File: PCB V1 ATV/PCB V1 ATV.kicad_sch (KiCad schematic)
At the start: 19 parts, among them J1 Power, J10 NW Sensor, J11 N Sensor, J12 NE Sensor, J13 SW Sensor, J14 S Sensor, J15 SE Sensor, J16 Joystick, J17 MotorControl, J2 PWM, J3 Analog, J4 PWM, J5 Analog, J6 Communication, J7 Digital, J8 Battery 12vIN, J9 Motor Controller, SW1 EStop, U1 L7809

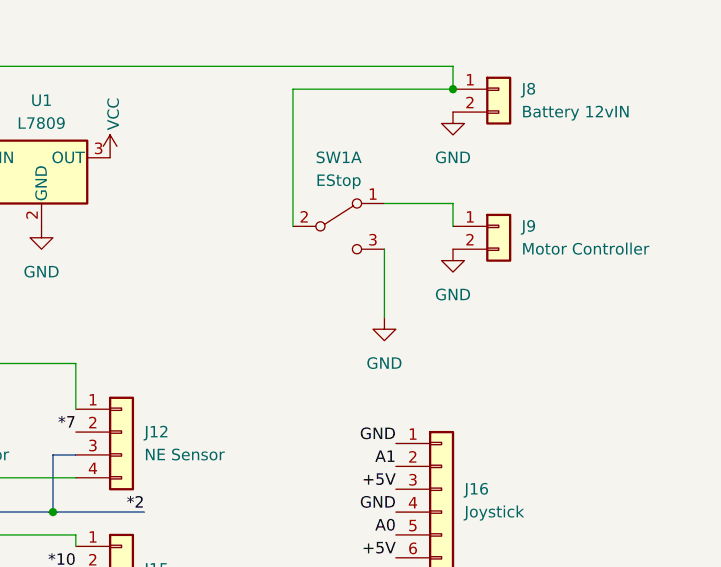
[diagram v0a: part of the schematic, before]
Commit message: V2.0
Added resistor between estop and ground
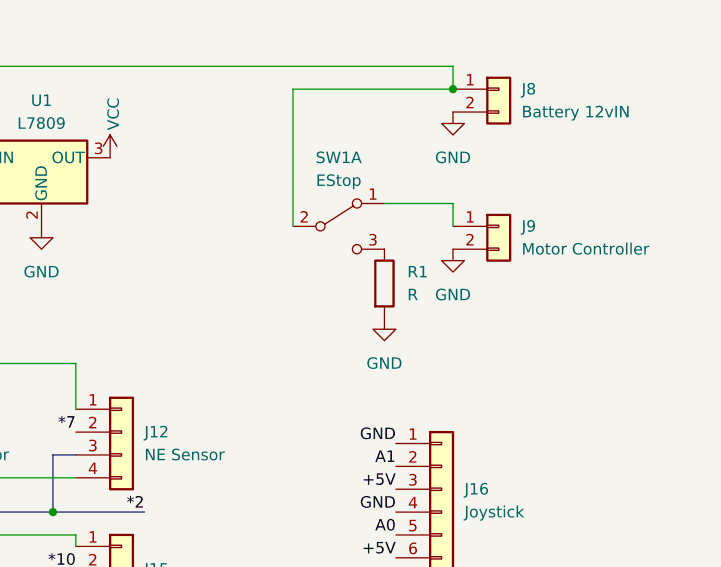
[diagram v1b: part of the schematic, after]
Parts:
- added R1: R, Resistor_THT:R_Axial_DIN0204_L3.6mm_D1.6mm_P7.62mm_Horizontal, symbol Device:R
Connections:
- net GND: now also R1.2; no longer SW1.3 (C)
- new net: R1.1, SW1.3 (C)
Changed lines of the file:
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@@
     (stroke (width 0) (type solid))
-  )
-  (wire (pts (xy 201.93 60.96) (xy 201.93 53.34))
-    (stroke (width 0) (type default))
   )
   (bus (pts (xy 165.1 76.2) (xy 167.64 76.2))
@@
         )
       )
+    )
+  )
+  (symbol (lib_id "Device:R") (at 201.93 57.15 0) (unit 1)
+    (in_bom yes) (on_board yes) (dnp no) (fields_autoplaced)
+    (property "Reference" "R1" (at 204.47 55.88 0)
+      (effects (font (size 1.27 1.27)) (justify left))
+    )
+    (property "Value" "R" (at 204.47 58.42 0)
+      (effects (font (size 1.27 1.27)) (justify left))
+    )
+    (property "Footprint" "Resistor_THT:R_Axial_DIN0204_L3.6mm_D1.6mm_P7.62mm_Horizontal" (at 200.152 57.15 90)
+      (effects (font (size 1.27 1.27)) hide)
+    )
+    (property "Datasheet" "~" (at 201.93 57.15 0)
+      (effects (font (size 1.27 1.27)) hide)
+    )
+    (pin "1")
+    (pin "2")
+    (instances
+      (project "PCB V1 ATV"
+        (path "/e63e39d7-6ac0-4ffd-8aa3-1841a4541b55"
+          (reference "R1") (unit 1)
+        )
+      )

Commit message: V1.2
Updated the board to fit the 2 part phoenix connectors, added a resistor, and added more silkscreen. Also removed .gbr and .drl files
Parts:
- J8, J9: footprint Connector_Phoenix_MC_HighVoltage:PhoenixContact_MCV_1,5_2-G-5.08_1x02_P5.08mm_Vertical -> Custom:Custom 2 Part Phoenix Connector
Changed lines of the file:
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@@
       (effects (font (size 1.27 1.27)) (justify left))
     )
-    (property "Footprint" "Connector_Phoenix_MC_HighVoltage:PhoenixContact_MCV_1,5_2-G-5.08_1x02_P5.08mm_Vertical" (at 214.63 50.8 0)
+    (property "Footprint" "Custom:Custom 2 Part Phoenix Connector" (at 214.63 50.8 0)
       (effects (font (size 1.27 1.27)) hide)
     )
@@
       (effects (font (size 1.27 1.27)) (justify left))
     )
-    (property "Footprint" "Connector_Phoenix_MC_HighVoltage:PhoenixContact_MCV_1,5_2-G-5.08_1x02_P5.08mm_Vertical" (at 214.63 35.56 0)
-      (effects (font (size 1.27 1.27)) hide)
-    )
+    (property "Footprint" "Custom:Custom 2 Part Phoenix Connector" (at 214.63 35.56 0)
+      (effects (font (size 1.27 1.27)) hide)
+    )
